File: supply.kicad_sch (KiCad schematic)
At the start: 104 parts, among them J12 Molex_Nano-Fit-105430_xx02-ho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, Q11 NX138BKMYL, Q12 NX138BKMYL, Q13 BCM857BS-7-F, Q14 BCM857BS-7-F, Q15 SSM3J332R, Q16 SSM3J332R, Q17 NX138BKMYL, Q18 SSM3J332R, Q19 NX138BKMYL, Q20 NX138BKMYL, Q21 NX138BKMYL, SW1 PCM12SMTR, U37 74LVC2G14GV, U38 74LVC1G175GV, U39 MP2386GG-P, U40 MP2386GG-P, U41 TPS7B8133DRVR, U42 TPS7A0518PDBVT

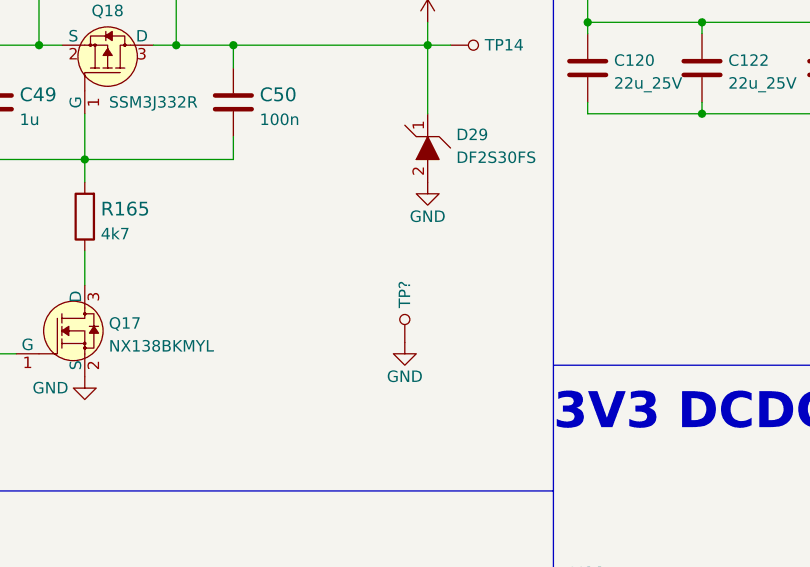
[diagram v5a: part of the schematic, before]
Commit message: Improved HDMI/DP length matching
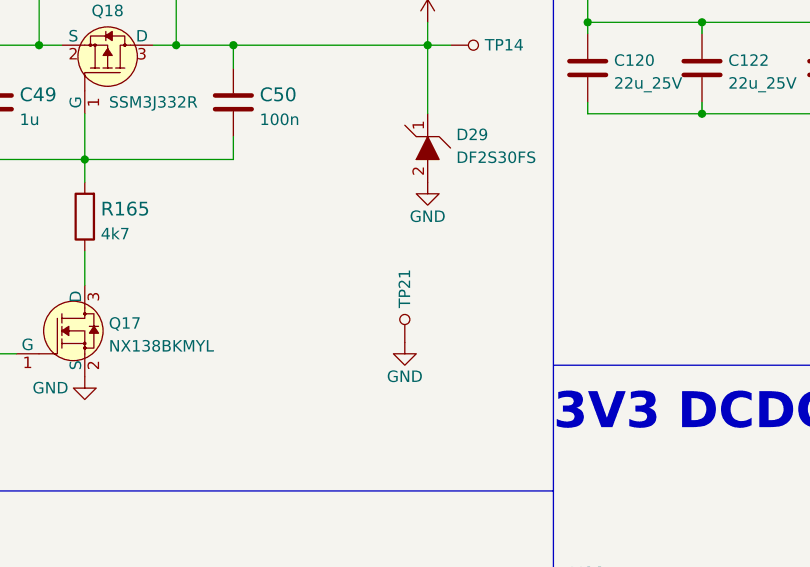
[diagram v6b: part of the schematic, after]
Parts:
- gave numbers to parts that had none: 1
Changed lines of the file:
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@@
   (symbol (lib_id "power:GND") (at 203.2 162.56 0) (mirror y) (unit 1)
     (in_bom yes) (on_board yes) (fields_autoplaced)
-    (property "Reference" "#PWR?" (id 0) (at 203.2 168.91 0)
+    (property "Reference" "#PWR0178" (id 0) (at 203.2 168.91 0)
       (effects (font (size 1.27 1.27)) hide)
     )
@@
   (symbol (lib_id "antmicroTestPoints:TP_SMD_0_75MM") (at 203.2 160.02 180) (unit 1)
     (in_bom yes) (on_board yes)
-    (property "Reference" "TP?" (id 0) (at 203.2 158.75 90)
-      (effects (font (size 1.27 1.27)) (justify right))
-    )
+    (property "Reference" "TP21" (id 0) (at 203.2 158.75 90)
+      (effects (font (size 1.27 1.27)) (justify right))
+    )

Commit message: CSchematic changes after review
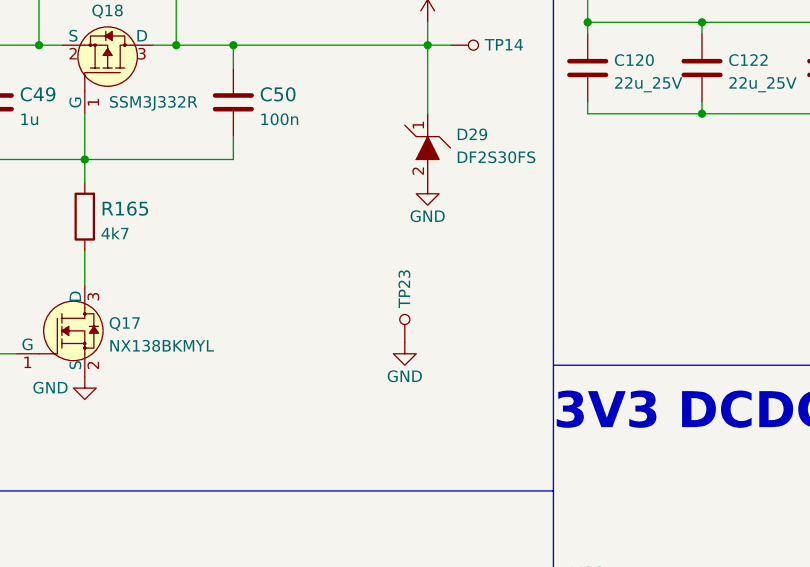
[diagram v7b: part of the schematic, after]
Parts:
- renumbered TP21 to TP23
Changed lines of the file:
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@@
   (symbol (lib_id "antmicroTestPoints:TP_SMD_0_75MM") (at 203.2 160.02 180) (unit 1)
     (in_bom yes) (on_board yes)
-    (property "Reference" "TP21" (id 0) (at 203.2 158.75 90)
+    (property "Reference" "TP23" (id 0) (at 203.2 158.75 90)
       (effects (font (size 1.27 1.27)) (justify right))
     )

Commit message: Loclib
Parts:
- C116, C117, C137: footprint antmicro-footprints:0402-cap -> jetson-orin-baseboard-footprints:0402-cap; symbol antmicroCapacitors0402:C_10u_0402 -> jetson-orin-baseboard:C_10u_0402
- C118, C119, C124, C50: footprint antmicro-footprints:0402-cap -> jetson-orin-baseboard-footprints:0402-cap; symbol antmicroCapacitors0402:C_100n_0402 -> jetson-orin-baseboard:C_100n_0402
- C120, C121, C122, C123, C125, C126: footprint antmicro-footprints:0805-cap -> jetson-orin-baseboard-footprints:0805-cap; symbol antmicroCapacitorsmisc:C_22u_0805_25V -> jetson-orin-baseboard:C_22u_0805_25V
- C127, C128: footprint antmicro-footprints:0402-cap -> jetson-orin-baseboard-footprints:0402-cap; symbol antmicroCapacitorsmisc:C_100n_0402_50V -> jetson-orin-baseboard:C_100n_0402_50V
- C129, C130, C142, C49: footprint antmicro-footprints:0402-cap -> jetson-orin-baseboard-footprints:0402-cap; symbol antmicroCapacitors0402:C_1u_0402 -> jetson-orin-baseboard:C_1u_0402
- C132, C133: footprint antmicro-footprints:0402-cap -> jetson-orin-baseboard-footprints:0402-cap; symbol antmicroCapacitors0402:C_220n_0402 -> jetson-orin-baseboard:C_220n_0402
- C134: footprint antmicro-footprints:0603-cap -> jetson-orin-baseboard-footprints:0603-cap; symbol antmicroCapacitors0603:C_10u_25V_0603 -> jetson-orin-baseboard:C_10u_25V_0603
- C135, C136: footprint antmicro-footprints:0402-cap -> jetson-orin-baseboard-footprints:0402-cap; symbol antmicroCapacitors0402:C_33p_0402 -> jetson-orin-baseboard:C_33p_0402
- C138, C139, C140, C141, C143, C144, C83: footprint antmicro-footprints:0402-cap -> jetson-orin-baseboard-footprints:0402-cap; symbol antmicroCapacitors0402:C_22u_0402 -> jetson-orin-baseboard:C_22u_0402
- D28, D29: footprint antmicro-footprints:SOD-923 -> jetson-orin-baseboard-footprints:SOD-923; symbol antmicroTVSDiodes:DF2S30FS -> jetson-orin-baseboard:DF2S30FS
- D30, D31, D32, D33: footprint antmicro-footprints:SOD-923 -> jetson-orin-baseboard-footprints:SOD-923; symbol antmicroTVSDiodes:ESD9X5.0ST5G -> jetson-orin-baseboard:ESD9X5.0ST5G
- D36, D37: footprint antmicro-footprints:SOD-523 -> jetson-orin-baseboard-footprints:SOD-523; symbol antmicroDiodesRectifiersSingle:RB521S30T1G -> jetson-orin-baseboard:RB521S30T1G
- J12: footprint antmicro-footprints:Molex_Nano-Fit_105430-xx02_1x02_P2.50mm_Horizontal_SMD -> jetson-orin-baseboard-footprints:Molex_Nano-Fit_105430-xx02_1x02_P2.50mm_Horizontal_SMD; symbol antmicroRectangularConnectorsHeadersFemalePins:Molex_Nano-Fit-105430_xx02-horizontal -> jetson-orin-baseboard:Molex_Nano-Fit-105430_xx02-horizontal
- L1, L2: footprint antmicro-footprints:IHLP2525CZER -> jetson-orin-baseboard-footprints:IHLP2525CZER; symbol antmicroFixedInductors:IHLP2525CZER2R2M01 -> jetson-orin-baseboard:IHLP2525CZER2R2M01
- Q11, Q12, Q17, Q19, Q20, Q21: footprint antmicro-footprints:DFN1006-3 -> jetson-orin-baseboard-footprints:DFN1006-3; symbol antmicroTransistorsFETsMOSFETsSingle:NX138BKMYL -> jetson-orin-baseboard:NX138BKMYL
- Q13, Q14: footprint antmicro-footprints:SOT-363 -> jetson-orin-baseboard-footprints:SOT-363; symbol antmicroTransistorsBipolarArrays:BCM857BS-7-F -> jetson-orin-baseboard:BCM857BS-7-F
- Q15, Q16, Q18: footprint antmicro-footprints:SOT-23-3 -> jetson-orin-baseboard-footprints:SOT-23-3; symbol antmicroTransistorsFETsMOSFETsSingle:SSM3J332R -> jetson-orin-baseboard:SSM3J332R
- R159, R164, R165: footprint antmicro-footprints:0402-res -> jetson-orin-baseboard-footprints:0402-res; symbol antmicroResistors0402:R_4k7_0402 -> jetson-orin-baseboard:R_4k7_0402
- R175, R252, R253, R274, R275: footprint antmicro-footprints:1206-res -> jetson-orin-baseboard-footprints:1206-res; symbol antmicroResistorsmisc:R_0R_1206 -> jetson-orin-baseboard:R_0R_1206
- R249, R262, R266, R267: footprint antmicro-footprints:0402-res -> jetson-orin-baseboard-footprints:0402-res; symbol antmicroResistors0402:R_100k_0402 -> jetson-orin-baseboard:R_100k_0402
- R250, R251, R254, R255, R259: footprint antmicro-footprints:0402-res -> jetson-orin-baseboard-footprints:0402-res; symbol antmicroResistors0402:R_10k_0402 -> jetson-orin-baseboard:R_10k_0402
- R256: footprint antmicro-footprints:0402-res -> jetson-orin-baseboard-footprints:0402-res; symbol antmicroResistors0402:R_1k_0402 -> jetson-orin-baseboard:R_1k_0402
- R257, R258, R261: footprint antmicro-footprints:0402-res -> jetson-orin-baseboard-footprints:0402-res; symbol antmicroResistors0402:R_200k_0402 -> jetson-orin-baseboard:R_200k_0402
- R260, R263, R264, R268: footprint antmicro-footprints:0402-res -> jetson-orin-baseboard-footprints:0402-res; symbol antmicroResistors0402:R_0R_0402 -> jetson-orin-baseboard:R_0R_0402
- R265: footprint antmicro-footprints:0402-res -> jetson-orin-baseboard-footprints:0402-res; symbol antmicroResistors0402:R_5R6_0402 -> jetson-orin-baseboard:R_5R6_0402
- R269, R271: footprint antmicro-footprints:0402-res -> jetson-orin-baseboard-footprints:0402-res; symbol antmicroResistors0402:R_40k2_1%_0402 -> jetson-orin-baseboard:R_40k2_1%_0402
- R270: footprint antmicro-footprints:0402-res -> jetson-orin-baseboard-footprints:0402-res; symbol antmicroResistors0402:R_5k49_1%_0402 -> jetson-orin-baseboard:R_5k49_1%_0402
- R272: footprint antmicro-footprints:0402-res -> jetson-orin-baseboard-footprints:0402-res; symbol antmicroResistors0402:R_8k87_1%_0402 -> jetson-orin-baseboard:R_8k87_1%_0402
- R273, R276: footprint antmicro-footprints:0603-res -> jetson-orin-baseboard-footprints:0603-res; symbol antmicroResistors0603:R_0R_0603 -> jetson-orin-baseboard:R_0R_0603
- S4, S5: footprint antmicro-footprints:B3U-3000P -> jetson-orin-baseboard-footprints:B3U-3000P; symbol antmicroPushbuttonSwitches:B3U-3000PM -> jetson-orin-baseboard:B3U-3000PM
- SW1: footprint antmicro-footprints:PCM12SMTR -> jetson-orin-baseboard-footprints:PCM12SMTR; symbol antmicroSlideSwitches:PCM12SMTR -> jetson-orin-baseboard:PCM12SMTR
- TP14, TP23, TP48, TP49, TP50, TP51, TP52, TP53, TP54, TP55: footprint antmicro-footprints:Testpoint_smd_0_75mm -> jetson-orin-baseboard-footprints:Testpoint_smd_0_75mm; symbol antmicroTestPoints:TP_SMD_0_75MM -> jetson-orin-baseboard:TP_SMD_0_75MM
- U37: footprint antmicro-footprints:SOT23-6L -> jetson-orin-baseboard-footprints:SOT23-6L; symbol antmicroLogicBuffersDriversReceiversTransceivers:74LVC2G14GV -> jetson-orin-baseboard:74LVC2G14GV
- U38: footprint antmicro-footprints:SOT-23-6 -> jetson-orin-baseboard-footprints:SOT-23-6; symbol antmicroLogicGatesandInverters:74LVC1G175GV -> jetson-orin-baseboard:74LVC1G175GV
- U39, U40: footprint antmicro-footprints:QFN-11_2x2mm_P0.5mm -> jetson-orin-baseboard-footprints:QFN-11_2x2mm_P0.5mm; symbol antmicroDCDCConverters:MP2386GG-P -> jetson-orin-baseboard:MP2386GG-P
- U41: footprint antmicro-footprints:WSON6_TI_2x2mm -> jetson-orin-baseboard-footprints:WSON6_TI_2x2mm; symbol antmicroPMICVoltageRegulatorsLinear:TPS7B8133DRVR -> jetson-orin-baseboard:TPS7B8133DRVR
- U42: footprint antmicro-footprints:SOT-23-5 -> jetson-orin-baseboard-footprints:SOT-23-5; symbol antmicroPMICVoltageRegulatorsLinear:TPS7A0518PDBVT -> jetson-orin-baseboard:TPS7A0518PDBVT
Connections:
- net 5V0_BST: no longer U39.7 (BST)
- net 5V0_EN: no longer U39.11 (EN)
- net 5V0_FB: no longer U39.10 (FB)
- net 5V0_INT_VCC: no longer U39.8 (VCC)
- net 5V0_PG: no longer U39.5 (PG)
- net 5V0_SW: no longer U39.6 (SW)
- net GND: no longer U39.2 (PGND), U39.3 (PGND), U39.4 (PGND), U39.9 (AGND)
- net VCC: no longer U39.1 (VIN)
- net ~{SHUTDOWN_REQ}: no longer D37.1
- net at C117.1, D36.1, R257.2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: no longer D37.2
